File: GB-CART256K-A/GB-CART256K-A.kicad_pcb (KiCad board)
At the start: 2 copper layers, 51.4 x 61 mm, 26 parts, among them J1 Conn_02x05_Counter_Clockwise, J2 DNF, U1 LC4032ZE-XXTN48, U2 MIC5370, U3 AT49F002-xxJx

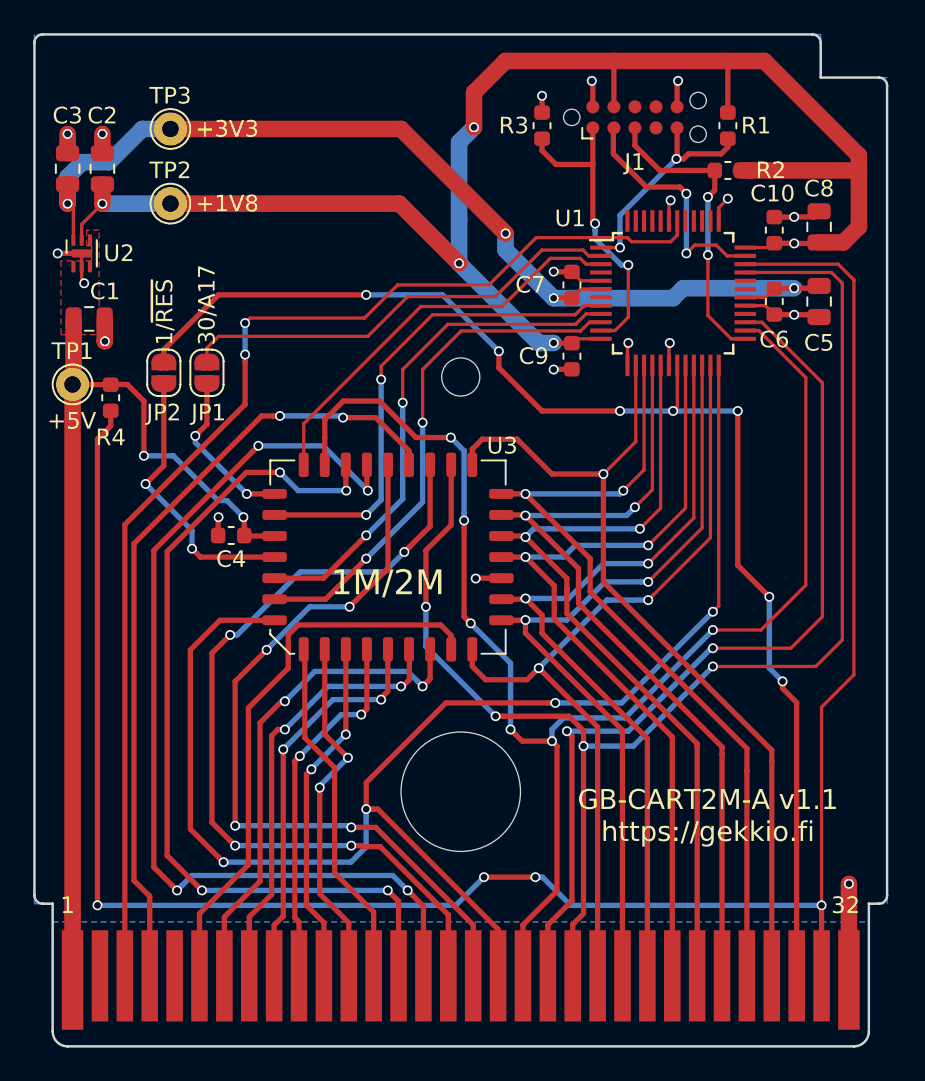
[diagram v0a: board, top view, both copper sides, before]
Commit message: Rename CART2M -> CART256K, update libs
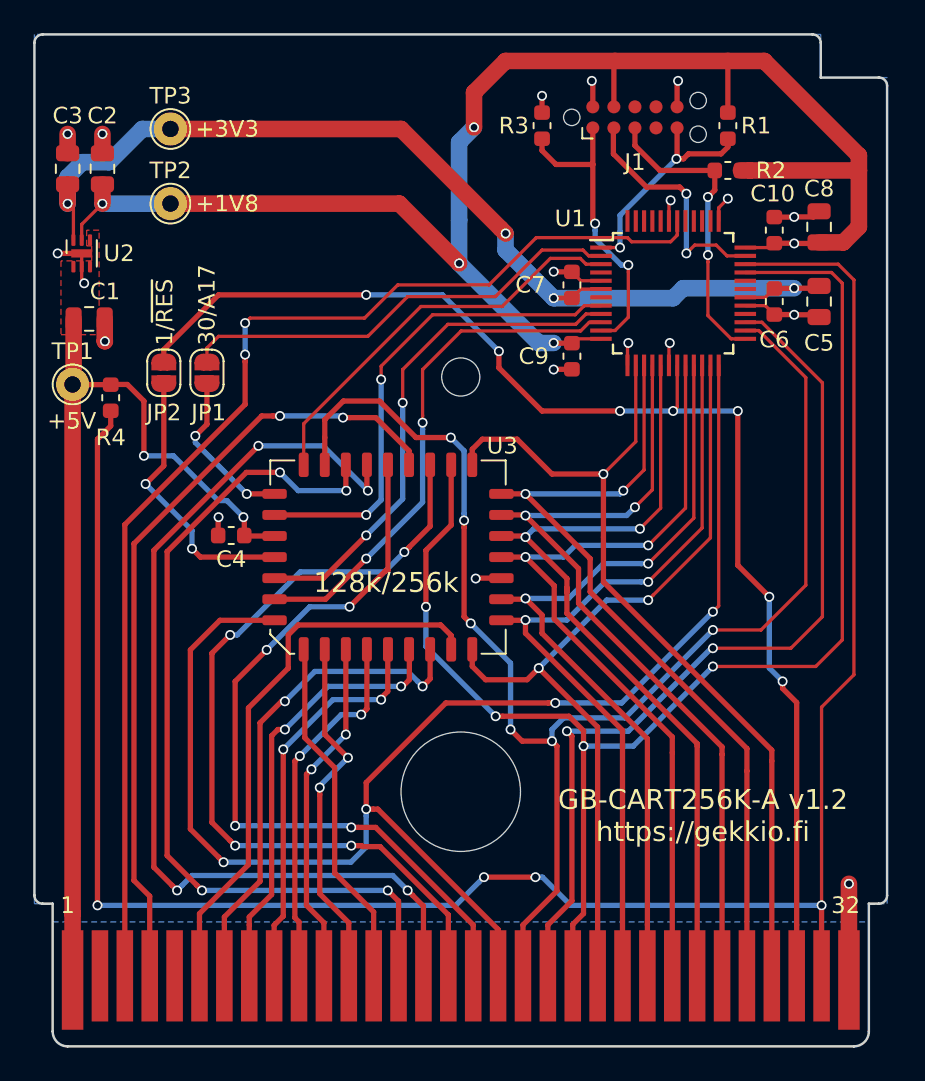
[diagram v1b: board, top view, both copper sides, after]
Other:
- board text added: "128k/256k"
- board text added: "GB-CART256K-A v1.2 https://gekkio.fi"
- board text removed: "1M/2M"
- board text removed: "GB-CART2M-A v1.1 https://gekkio.fi"
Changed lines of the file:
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@@
-(kicad_pcb (version 20171130) (host pcbnew 5.1.2-f72e74a~84~ubuntu19.04.1)
+(kicad_pcb (version 20171130) (host pcbnew 5.1.5-52549c5~84~ubuntu19.10.1)
   (general
     (thickness 1)
@@
   (page A4)
   (title_block
-    (title GB-CART2M-A)
-    (rev v1.1)
+    (title GB-CART256K-A)
+    (rev v1.2)
     (company https://gekkio.fi)
   )
@@
   (module Package_DFN_QFN:MLF-6-1EP_1.6x1.6mm_P0.5mm_EP0.5x1.26mm (layer F.Cu)
     (at 77.15 52.2 90)
-    (descr "MLF, 6 Pin (http://ww1.microchip.com/downloads/en/DeviceDoc/mic5353.pdf), generated with kicad-footprint-generator ipc_dfn_qfn_generator.py")
-    (tags "MLF DFN_QFN")
+    (descr "MLF, 6 Pin (http://ww1.microchip.com/downloads/en/DeviceDoc/mic5353.pdf), generated with kicad-footprint-generator ipc_noLead_generator.py")
+    (tags "MLF NoLead")
     (attr smd)
     (fp_text reference U2 (at 0 2.25 180) (layer F.SilkS)
@@
     (fp_line (start -0.8 0.91) (end 0.8 0.91) (layer F.SilkS) (width 0.12))
     (fp_line (start 0 -0.91) (end 0.8 -0.91) (layer F.SilkS) (width 0.12))
+    (pad "" smd roundrect (at 0 0.315 90) (size 0.4 0.51) (layers F.Paste) (roundrect_rratio 0.25))
+    (pad "" smd roundrect (at 0 -0.315 90) (size 0.4 0.51) (layers F.Paste) (roundrect_rratio 0.25))
+    (pad 7 smd rect (at 0 0 90) (size 0.5 1.26) (layers F.Cu F.Mask)
+      (net 5 GND))
     (pad 6 smd roundrect (at 0.8 -0.5 90) (size 0.7 0.25) (layers F.Cu F.Paste F.Mask) (roundrect_rratio 0.25)
       (net 3 +3V3))
@@
     (pad 1 smd roundrect (at -0.8 -0.5 90) (size 0.7 0.25) (layers F.Cu F.Paste F.Mask) (roundrect_rratio 0.25)
       (net 2 +5V))
-    (pad "" smd roundrect (at 0 0.315 90) (size 0.4 0.51) (layers F.Paste) (roundrect_rratio 0.25))
-    (pad "" smd roundrect (at 0 -0.315 90) (size 0.4 0.51) (layers F.Paste) (roundrect_rratio 0.25))
-    (pad 7 smd roundrect (at 0 0 90) (size 0.5 1.26) (layers F.Cu F.Mask) (roundrect_rratio 0.25)
-      (net 5 GND))
     (model ${KISYS3DMOD}/Package_DFN_QFN.3dshapes/MLF-6-1EP_1.6x1.6mm_P0.5mm_EP0.5x1.26mm.wrl
       (at (xyz 0 0 0))
@@
   (gr_arc (start 76.3 99.1) (end 75.4 99.1) (angle -90) (layer Edge.Cuts) (width 0.15))
   (gr_arc (start 123.7 99.1) (end 123.7 100) (angle -90) (layer Edge.Cuts) (width 0.15))
-  (gr_text 1M/2M (at 95.6 72.05) (layer F.SilkS)
-    (effects (font (size 1.5 1.5) (thickness 0.3)))
+  (gr_text 128k/256k (at 95.5 72.05) (layer F.SilkS)
+    (effects (font (size 1.2 1.2) (thickness 0.3)))
   )
   (gr_text +5V (at 76.55 62.3) (layer F.SilkS)
@@
     (effects (font (size 1 1) (thickness 0.15)) (justify left))
   )
-  (gr_text "GB-CART2M-A v1.1\nhttps://gekkio.fi" (at 114.9 86.1) (layer F.SilkS)
+  (gr_text "GB-CART256K-A v1.2\nhttps://gekkio.fi" (at 114.6 86.1) (layer F.SilkS)
     (effects (font (size 1.2 1.2) (thickness 0.2)))
   )

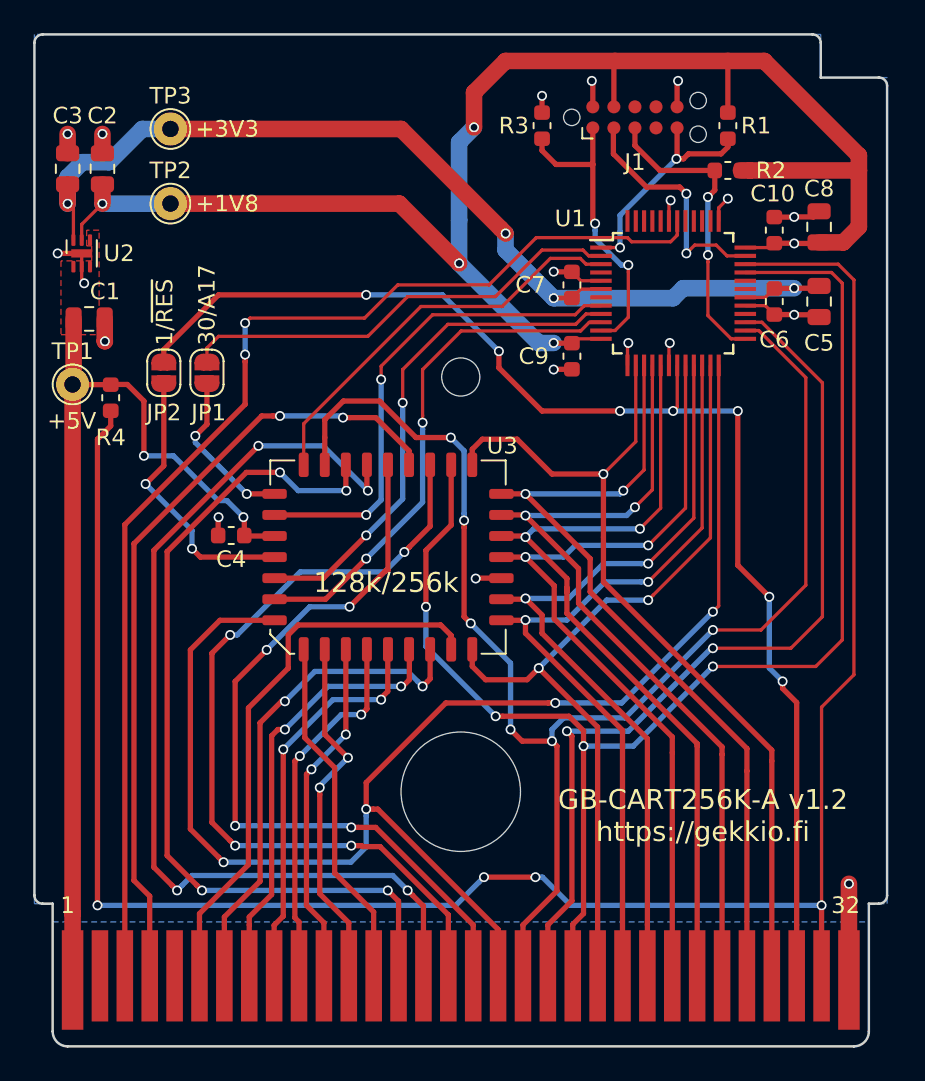
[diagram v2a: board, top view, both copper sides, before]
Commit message: Upgrade most projects to KiCad 6
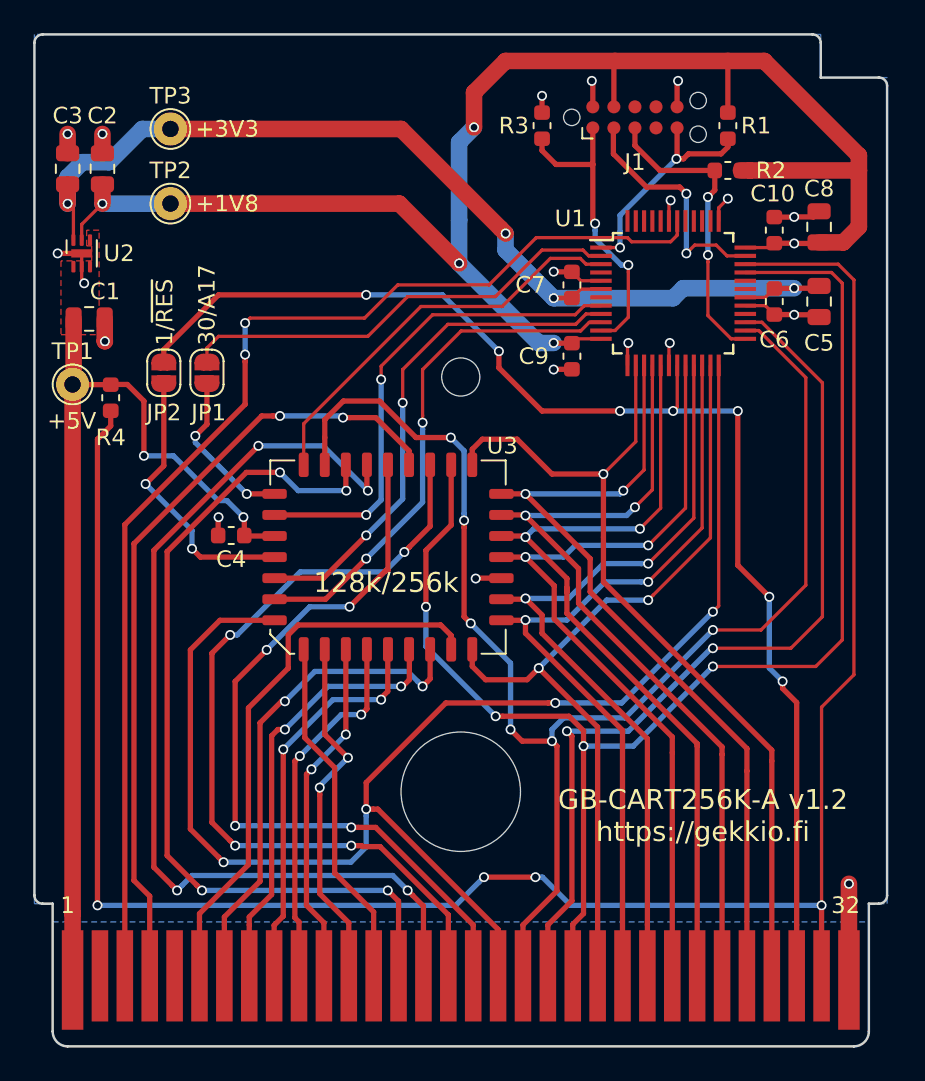
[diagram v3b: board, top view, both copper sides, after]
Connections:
- net /~PRG renamed /~{PRG}
- net /~RD renamed /~{RD}
- net /~RES renamed /~{RES}
- net /~RWR renamed /~{RWR}
- net /~WR renamed /~{WR}
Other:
- net class Default removed
- board text added: "1/~{RES}"
- board text removed: "1/~RES"
